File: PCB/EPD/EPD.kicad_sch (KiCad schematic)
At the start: 68 parts, among them J1 Conn_01x26, J2 Shelly, J3 USB-PROG, J4 BTN1, J6 BTN2, J7 USB-C-Socket-V, J8 PWR, P1 +, P10 2, P11 1, P12 1, P2 -, P3 2, P4 2, P5 1, P6 1, P7 +, P8 -, P9 2, Q1 BSS138, U2 ESP32-S3-MINI-1, U3 MD8942

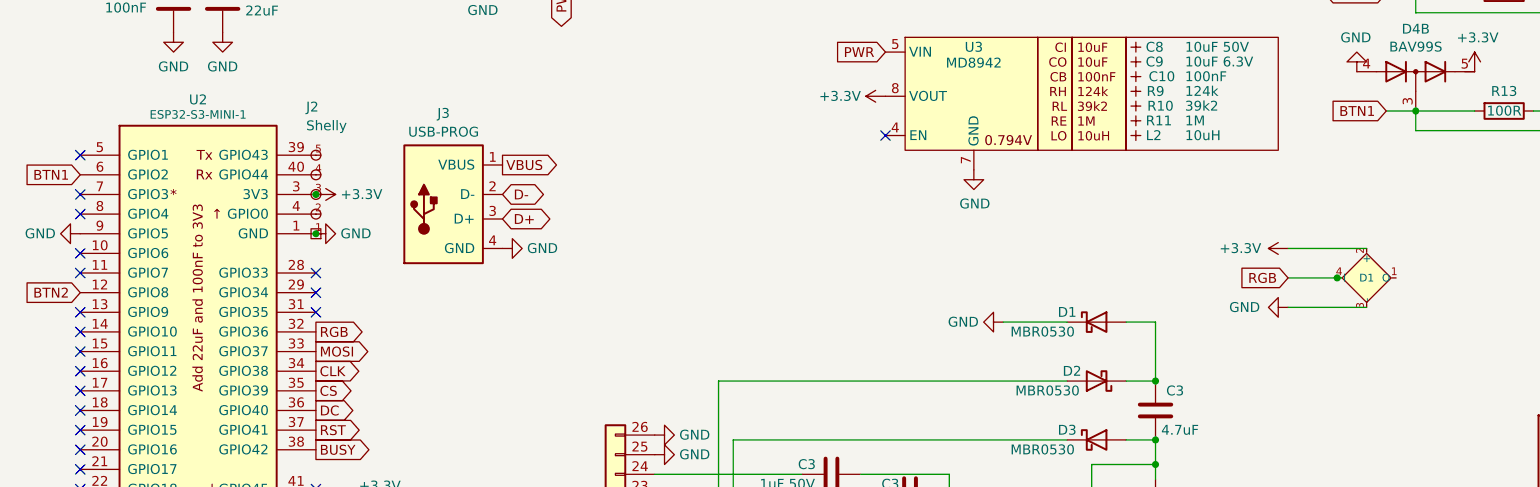
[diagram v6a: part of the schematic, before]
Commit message: FPC centred and retracked
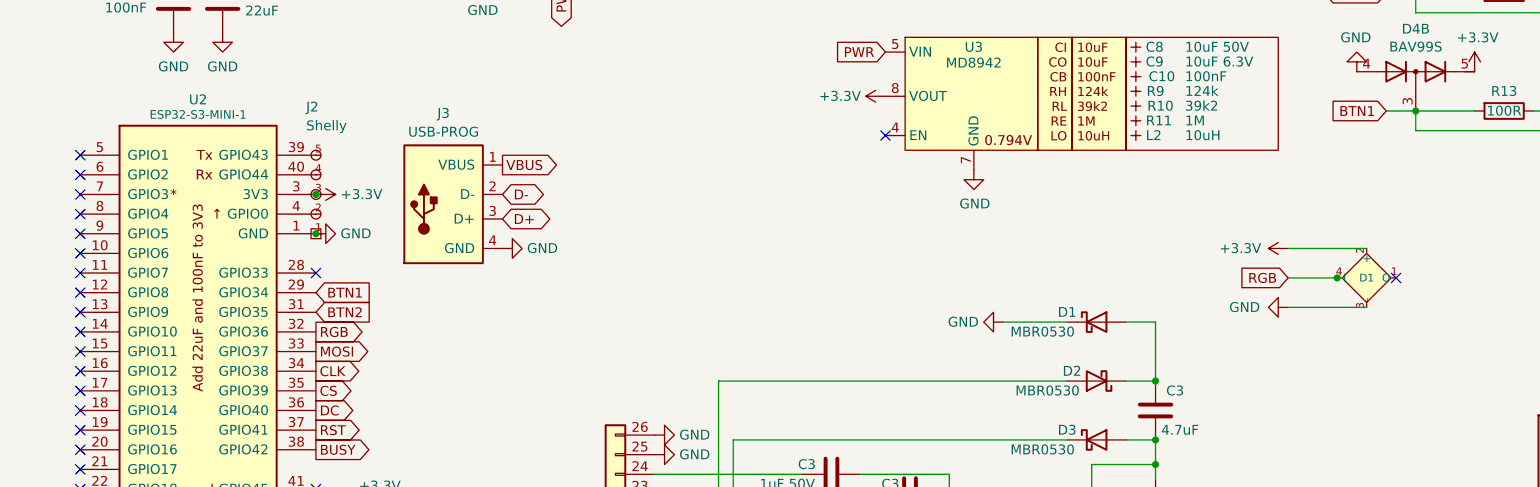
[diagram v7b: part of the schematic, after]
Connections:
- net BTN1: now also U2.29 (GPIO34); no longer U2.6 (GPIO2)
- net BTN2: now also U2.31 (GPIO35); no longer U2.12 (GPIO8)
- net GND: no longer U2.9 (GPIO5)
- no-connect marks 27 -> 29
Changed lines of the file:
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@@
   (no_connect (at 123.19 135.255))
   (no_connect (at 48.895 91.44))
+  (no_connect (at 219.075 64.135))
   (no_connect (at 48.895 48.26))
   (no_connect (at 79.375 91.44))
   (no_connect (at 79.375 99.06))
-  (no_connect (at 79.375 96.52))
   (no_connect (at 153.035 45.72))
   (no_connect (at 48.895 53.34))
+  (no_connect (at 48.895 50.8))
   (no_connect (at 48.895 81.28))
   (no_connect (at 48.895 88.9))
   (no_connect (at 48.895 83.82))
   (no_connect (at 48.895 71.12))
-  (no_connect (at 79.375 68.58))
+  (no_connect (at 48.895 99.06))
   (no_connect (at 123.19 132.715))
   (no_connect (at 48.895 68.58))
-  (no_connect (at 48.895 99.06))
+  (no_connect (at 48.895 58.42))
   (no_connect (at 79.375 93.98))
-  (no_connect (at 79.375 66.04))
+  (no_connect (at 48.895 66.04))
+  (no_connect (at 79.375 96.52))
   (no_connect (at 79.375 63.5))
   (no_connect (at 48.895 60.96))
@@
     )
   )
-  (global_label "BTN2" (shape input) (at 48.895 66.04 180) (fields_autoplaced)
-    (effects (font (size 1.27 1.27)) (justify right))
-    (property "Intersheetrefs" "${INTERSHEET_REFS}" (at 41.7864 66.04 0)
-      (effects (font (size 1.27 1.27)) (justify right) hide)
+  (global_label "BTN2" (shape input) (at 79.375 68.58 0) (fields_autoplaced)
+    (effects (font (size 1.27 1.27)) (justify left))
+    (property "Intersheetrefs" "${INTERSHEET_REFS}" (at 86.4836 68.58 0)
+      (effects (font (size 1.27 1.27)) (justify left) hide)
     )
   )
@@
     )
   )
-  (global_label "BTN1" (shape input) (at 48.895 50.8 180) (fields_autoplaced)
-    (effects (font (size 1.27 1.27)) (justify right))
-    (property "Intersheetrefs" "${INTERSHEET_REFS}" (at 41.7864 50.8 0)
-      (effects (font (size 1.27 1.27)) (justify right) hide)
+  (global_label "BTN1" (shape input) (at 79.375 66.04 0) (fields_autoplaced)
+    (effects (font (size 1.27 1.27)) (justify left))
+    (property "Intersheetrefs" "${INTERSHEET_REFS}" (at 86.4836 66.04 0)
+      (effects (font (size 1.27 1.27)) (justify left) hide)
     )
   )
@@
         )
       )
-    )
-  )
-  (symbol (lib_id "power:GND") (at 48.895 58.42 270) (unit 1)
-    (in_bom yes) (on_board yes) (dnp no) (fields_autoplaced)
-    (property "Reference" "#PWR01" (at 42.545 58.42 0)
-      (effects (font (size 1.27 1.27)) hide)
-    )
-    (property "Value" "GND" (at 45.7201 58.42 90)
-      (effects (font (size 1.27 1.27)) (justify right))
-    )
-    (property "Footprint" "" (at 48.895 58.42 0)
-      (effects (font (size 1.27 1.27)) hide)
-    )
-    (property "Datasheet" "" (at 48.895 58.42 0)
-      (effects (font (size 1.27 1.27)) hide)
-    )
-    (pin "1")
-    (instances
-      (project "USBA"
-        (path "/2d210a96-f81f-42a9-8bf4-1b43c11086f3"
-          (reference "#PWR01") (unit 1)
-        )
-      )
-      (project "EPD"
-        (path "/46c350bb-7de4-4e81-aafd-4af55e37aab0"
-          (reference "#PWR021") (unit 1)
-        )
-      )

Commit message: BTN added
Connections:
- net at R1.1: now also JP1.3 (B); no longer JP1.1 (A)
- net at R1.2: now also JP1.1 (A); no longer JP1.3 (B)
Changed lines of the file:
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@@
     )
   )
-  (symbol (lib_id "Jumper:SolderJumper_3_Bridged12") (at 183.515 146.05 270) (mirror x) (unit 1)
+  (symbol (lib_id "Jumper:SolderJumper_3_Bridged12") (at 183.515 146.05 270) (unit 1)
     (in_bom no) (on_board yes) (dnp no)
     (property "Reference" "JP1" (at 185.1659 146.05 90)
